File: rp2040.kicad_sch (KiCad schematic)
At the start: 39 parts, among them U10 PJ-320A, U11 RP2040, U12 XC6206PxxxMR, U13 USB Boot, U14 USBLC6-2SC6, U15 Reset, U16 W25Q16JVUXIQ, U9 TYPE-C-31-M-12, Y2 12MHz - 20pF

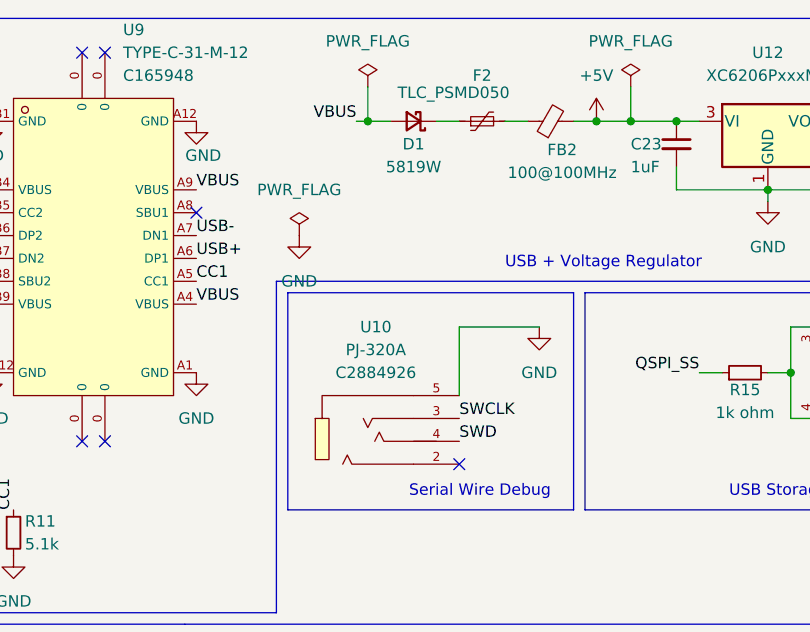
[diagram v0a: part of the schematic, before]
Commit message: Replace the SWD TRRS connector with a simple header pin connector
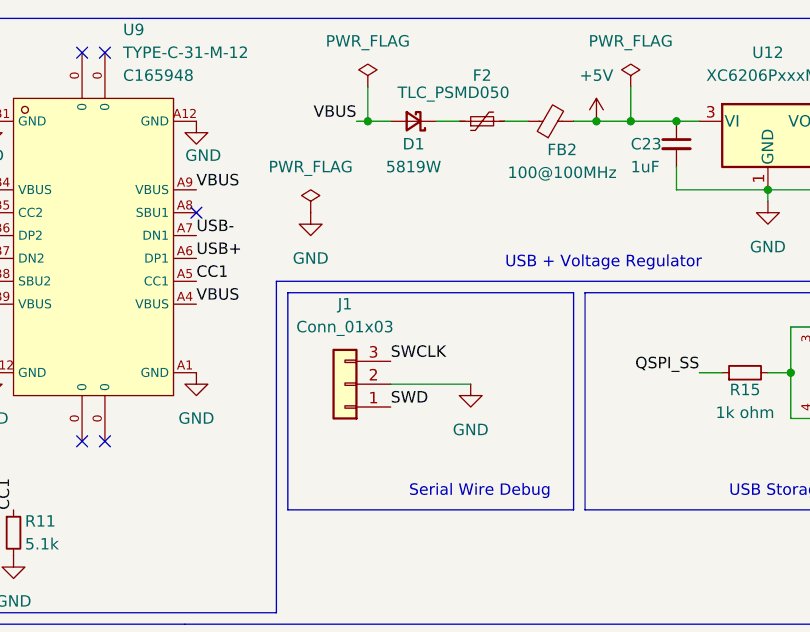
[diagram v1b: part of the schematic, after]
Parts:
- removed U10: PJ-320A, footprints:trrs-connector-pj320a, symbol trrs-connector-pj320a:PJ-320A
- added J1: Conn_01x03, Connector_PinHeader_2.54mm:PinHeader_1x03_P2.54mm_Vertical, symbol Connector_Generic:Conn_01x03
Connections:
- net GND: now also J1.2 (Pin_2)
- net SWCLK: now also J1.3 (Pin_3)
- net SWD: now also J1.1 (Pin_1)
- no-connect marks 8 -> 7
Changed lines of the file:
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@@
 	)
 	(no_connect
-		(at 74.93 62.23)
-	)
-	(no_connect
 		(at 22.86 41.91)
 	)
@@
 	(wire
 		(pts
-			(xy 74.93 46.99) (xy 74.93 54.61)
-		)
-		(stroke
-			(width 0)
-			(type default)
-		)
-	)
-	(wire
-		(pts
 			(xy 146.05 49.53) (xy 151.13 49.53)
 		)
@@
 		)
 	)
+	(wire
+		(pts
+			(xy 67.31 53.34) (xy 76.2 53.34)
+		)
+		(stroke
+			(width 0)
+			(type default)
+		)
+	)
 	(polyline
 		(pts
@@
 	(wire
 		(pts
-			(xy 83.82 46.99) (xy 74.93 46.99)
-		)
-		(stroke
-			(width 0)
-			(type default)
-		)
-	)
-	(wire
-		(pts
 			(xy 121.92 46.99) (xy 124.46 46.99)
 		)
@@
 	)
 	(label "SWD"
-		(at 74.93 59.69 0)
+		(at 67.31 55.88 0)
 		(effects
 			(font
@@
 	)
 	(label "SWCLK"
-		(at 74.93 57.15 0)
+		(at 67.31 50.8 0)
 		(effects
 			(font
@@
 	)
 	(symbol
+		(lib_id "Connector_Generic:Conn_01x03")
+		(at 62.23 53.34 180)
+		(unit 1)
+		(exclude_from_sim no)
+		(in_bom yes)
+		(on_board yes)
+		(dnp no)
+		(fields_autoplaced yes)
+		(property "Reference" "J1"
+			(at 62.23 44.45 0)
+			(effects
+				(font
+					(size 1.27 1.27)
+				)
+			)
+		)
+		(property "Value" "Conn_01x03"
+			(at 62.23 46.99 0)
+			(effects
+				(font
+					(size 1.27 1.27)
+				)
+			)
+		)
+		(property "Footprint" "Connector_PinHeader_2.54mm:PinHeader_1x03_P2.54mm_Vertical"
+			(at 62.23 53.34 0)
+			(effects
+				(font
+					(size 1.27 1.27)
+				)
+				(hide yes)
+			)
+		)
+		(property "Datasheet" "~"
+			(at 62.23 53.34 0)
+			(effects
+				(font
+					(size 1.27 1.27)
+				)
+				(hide yes)
+			)
+		)
+		(property "Description" "Generic connector, single row, 01x03, script generated (kicad-library-utils/schlib/autogen/connector/)"
+			(at 62.23 53.34 0)
+			(effects
+				(font
+					(size 1.27 1.27)
+				)
+				(hide yes)
+			)
+		)
+		(pin "1"
+		)
+		(pin "2"
+		)
+		(pin "3"
+		)
+		(instances
+			(project ""
+				(path "/bab9d4ba-4671-4f57-a245-5e0527b464d7/59d9fd80-c3ab-4343-9591-286205d42abc"
+					(reference "J1")
+					(unit 1)
+				)
+			)
+		)
+	)
+	(symbol
 		(lib_id "Device:C_Small")
 		(at 195.58 22.86 0)
@@
 	(symbol
 		(lib_id "power:GND")
-		(at 57.15 36.83 0)
+		(at 58.42 34.29 0)
 		(unit 1)
 		(exclude_from_sim no)
@@
 		(fields_autoplaced yes)
 		(property "Reference" "#PWR02"
-			(at 57.15 43.18 0)
+			(at 58.42 40.64 0)
 			(effects
 				(font
@@
 		)
 		(property "Value" "GND"
-			(at 57.15 41.91 0)
+			(at 58.42 39.37 0)
 			(effects
 				(font
@@
 		)
 		(property "Footprint" ""
-			(at 57.15 36.83 0)
+			(at 58.42 34.29 0)
 			(effects
 				(font
@@
 		)
 		(property "Datasheet" ""
-			(at 57.15 36.83 0)
+			(at 58.42 34.29 0)
 			(effects
 				(font
@@
 		)
 		(property "Description" "Power symbol creates a global label with name \"GND\" , ground"
-			(at 57.15 36.83 0)
+			(at 58.42 34.29 0)
 			(effects
 				(font
@@
 	(symbol
 		(lib_id "power:GND")
-		(at 83.82 46.99 0)
+		(at 76.2 53.34 0)
 		(unit 1)
 		(exclude_from_sim no)
@@
 		(fields_autoplaced yes)
 		(property "Reference" "#PWR048"
-			(at 83.82 53.34 0)
+			(at 76.2 59.69 0)
 			(effects
 				(font
@@
 		)
 		(property "Value" "GND"
-			(at 83.82 52.07 0)
+			(at 76.2 58.42 0)
 			(effects
 				(font
@@
 		)
 		(property "Footprint" ""
-			(at 83.82 46.99 0)
+			(at 76.2 53.34 0)
 			(effects
 				(font
@@
 		)
 		(property "Datasheet" ""
-			(at 83.82 46.99 0)
+			(at 76.2 53.34 0)
 			(effects
 				(font
@@
 		)
 		(property "Description" "Power symbol creates a global label with name \"GND\" , ground"
-			(at 83.82 46.99 0)
+			(at 76.2 53.34 0)
 			(effects
 				(font
@@
 	(symbol
 		(lib_id "power:PWR_FLAG")
-		(at 57.15 36.83 0)
+		(at 58.42 34.29 0)
 		(unit 1)
 		(exclude_from_sim no)
@@
 		(fields_autoplaced yes)
 		(property "Reference" "#FLG03"
-			(at 57.15 34.925 0)
+			(at 58.42 32.385 0)
 			(effects
 				(font
@@
 		)
 		(property "Value" "PWR_FLAG"
-			(at 57.15 31.75 0)
+			(at 58.42 29.21 0)
 			(effects
 				(font
@@
 		)
 		(property "Footprint" ""
-			(at 57.15 36.83 0)
+			(at 58.42 34.29 0)
 			(effects
 				(font
@@
 		)
 		(property "Datasheet" "~"
-			(at 57.15 36.83 0)
+			(at 58.42 34.29 0)
 			(effects
 				(font
@@
 		)
 		(property "Description" "Special symbol for telling ERC where power comes from"
-			(at 57.15 36.83 0)
+			(at 58.42 34.29 0)
 			(effects
 				(font
@@
 					(unit 1)
 				)
-			)
-		)
-	)
-	(symbol
-		(lib_id "trrs-connector-pj320a:PJ-320A")
-		(at 72.39 44.45 0)
-		(unit 1)
-		(exclude_from_sim no)
-		(in_bom yes)
-		(on_board yes)
-		(dnp no)
-		(fields_autoplaced yes)
-		(property "Reference" "U10"
-			(at 65.659 46.99 0)
-			(effects
-				(font
-					(size 1.27 1.27)
-				)
-			)
-		)
-		(property "Value" "PJ-320A"
-			(at 65.659 49.53 0)
-			(effects
-				(font
-					(size 1.27 1.27)
-				)
-			)
-		)
-		(property "Footprint" "footprints:trrs-connector-pj320a"
-			(at 72.39 54.61 0)
-			(effects
-				(font
-					(size 1.27 1.27)
-					(italic yes)
-				)
-				(hide yes)
-			)
-		)
-		(property "Datasheet" "https://atta.szlcsc.com/upload/public/pdf/source/20211009/3530D3239D5E54DF713226555EC23A50.pdf"
-			(at 70.104 44.323 0)
-			(effects
-				(font
-					(size 1.27 1.27)
-				)
-				(justify left)
-				(hide yes)
-			)
-		)
-		(property "Description" ""
-			(at 72.39 44.45 0)
-			(effects
-				(font
-					(size 1.27 1.27)
-				)
-				(hide yes)
-			)
-		)
-		(property "LCSC" "C2884926"
-			(at 65.659 52.07 0)
-			(effects
-				(font
-					(size 1.27 1.27)
-				)
-			)
-		)
-		(pin "4"
-		)
-		(pin "3"
-		)
-		(pin "2"
-		)
-		(pin "5"
-		)
-		(instances
-			(project "rp2040-kicad-template"
-				(path "/bab9d4ba-4671-4f57-a245-5e0527b464d7/59d9fd80-c3ab-4343-9591-286205d42abc"
-					(reference "U10")
-					(unit 1)
-				)
